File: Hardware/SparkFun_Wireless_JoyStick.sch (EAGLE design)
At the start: 76 parts, among them J7 CORTEX_DEBUGPTH, Q1 2.5A/30V, U1 JOYSTICKPTH, U2 JOYSTICKPTH, U3 74AHC1G125, U4 AP2112K-3.3V, U5 XBEE-2B3, U6 MAX1704X, U7 MCP73831, U8 ATSAMD21G-A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

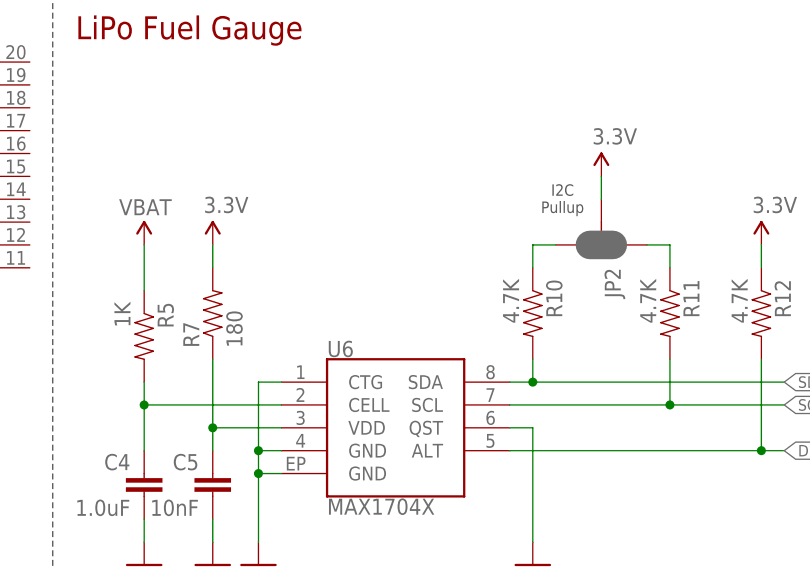
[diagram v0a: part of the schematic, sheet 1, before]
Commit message: Added fuel gauge i2c address
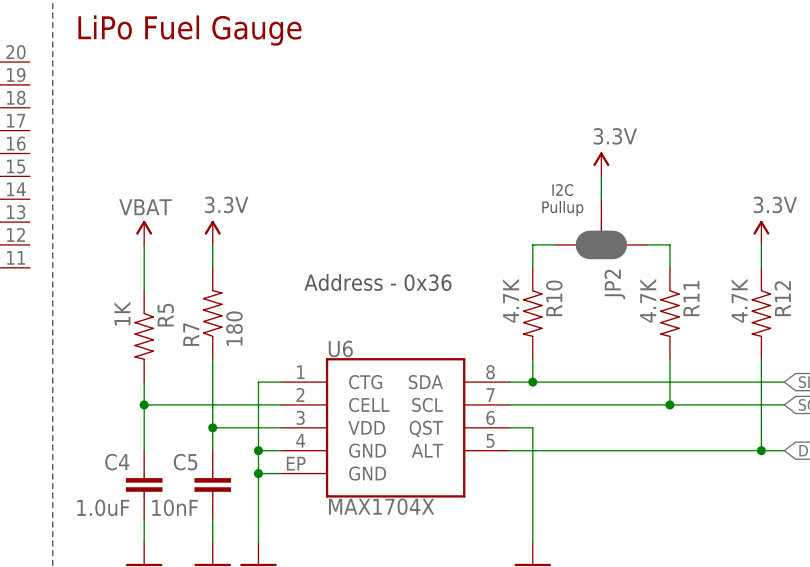
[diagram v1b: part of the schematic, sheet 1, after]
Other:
- note added: "Address - 0x36"
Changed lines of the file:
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@@
 <text x="193.04" y="137.16" size="1.27" layer="97" align="bottom-center">Charge Current
 Select</text>
+<text x="185.42" y="76.2" size="1.778" layer="97">Address - 0x36</text>
 </plain>
 <instances>

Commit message: Minor Changes
- added reset switch
- reversed power and ground on joysticks
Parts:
- added S8: MOMENTARY-SWITCH-SPST-SMD-4.6X2.8MM, SparkFun-Switches:MOMENTARY-SWITCH-SPST-SMD-4.6X2.8MM
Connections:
- net !RESET: now also S8.1
- net 3.3V: now also U1.H-, U1.V-, U2.H-, U2.V-; no longer U1.H+, U1.V+, U2.H+, U2.V+
- net GND: now also S8.2, U1.H+, U1.V+, U2.H+, U2.V+; no longer U1.H-, U1.V-, U2.H-, U2.V-
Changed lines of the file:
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@@
 <part name="SUPPLY23" library="SparkFun-Aesthetics" deviceset="VIN" device=""/>
 <part name="GND30" library="SparkFun-Aesthetics" deviceset="GND" device=""/>
+<part name="S8" library="SparkFun-Switches" deviceset="MOMENTARY-SWITCH-SPST" device="-SMD-4.6X2.8MM" value=""/>
+<part name="GND31" library="SparkFun-Aesthetics" deviceset="GND" device=""/>
 </parts>
 <sheets>
@@
 </segment>
 <segment>
-<pinref part="U2" gate="G$1" pin="V-"/>
-<wire x1="50.8" y1="106.68" x2="53.34" y2="106.68" width="0.1524" layer="91"/>
-<wire x1="53.34" y1="106.68" x2="53.34" y2="96.52" width="0.1524" layer="91"/>
-<pinref part="U2" gate="G$1" pin="H-"/>
-<wire x1="53.34" y1="96.52" x2="50.8" y2="96.52" width="0.1524" layer="91"/>
 <pinref part="U2" gate="G$1" pin="SEL-"/>
 <wire x1="50.8" y1="88.9" x2="53.34" y2="88.9" width="0.1524" layer="91"/>
-<wire x1="53.34" y1="88.9" x2="53.34" y2="96.52" width="0.1524" layer="91"/>
-<junction x="53.34" y="96.52"/>
 <wire x1="53.34" y1="88.9" x2="53.34" y2="81.28" width="0.1524" layer="91"/>
+<pinref part="GND5" gate="1" pin="GND"/>
+<pinref part="U2" gate="G$1" pin="V+"/>
+<wire x1="50.8" y1="111.76" x2="53.34" y2="111.76" width="0.1524" layer="91"/>
+<wire x1="53.34" y1="111.76" x2="53.34" y2="101.6" width="0.1524" layer="91"/>
+<pinref part="U2" gate="G$1" pin="H+"/>
+<wire x1="53.34" y1="101.6" x2="50.8" y2="101.6" width="0.1524" layer="91"/>
+<wire x1="53.34" y1="101.6" x2="53.34" y2="88.9" width="0.1524" layer="91"/>
+<junction x="53.34" y="101.6"/>
 <junction x="53.34" y="88.9"/>
-<pinref part="GND5" gate="1" pin="GND"/>
-</segment>
-<segment>
-<pinref part="U1" gate="G$1" pin="V-"/>
-<wire x1="20.32" y1="106.68" x2="22.86" y2="106.68" width="0.1524" layer="91"/>
-<wire x1="22.86" y1="106.68" x2="22.86" y2="96.52" width="0.1524" layer="91"/>
+</segment>
+<segment>
 <pinref part="U1" gate="G$1" pin="SEL-"/>
-<wire x1="22.86" y1="96.52" x2="22.86" y2="88.9" width="0.1524" layer="91"/>
 <wire x1="22.86" y1="88.9" x2="22.86" y2="81.28" width="0.1524" layer="91"/>
 <wire x1="20.32" y1="88.9" x2="22.86" y2="88.9" width="0.1524" layer="91"/>
+<pinref part="GND2" gate="1" pin="GND"/>
+<pinref part="U1" gate="G$1" pin="H+"/>
+<wire x1="20.32" y1="101.6" x2="22.86" y2="101.6" width="0.1524" layer="91"/>
+<wire x1="22.86" y1="101.6" x2="22.86" y2="111.76" width="0.1524" layer="91"/>
+<pinref part="U1" gate="G$1" pin="V+"/>
+<wire x1="22.86" y1="111.76" x2="20.32" y2="111.76" width="0.1524" layer="91"/>
+<wire x1="22.86" y1="101.6" x2="22.86" y2="88.9" width="0.1524" layer="91"/>
+<junction x="22.86" y="101.6"/>
 <junction x="22.86" y="88.9"/>
-<pinref part="U1" gate="G$1" pin="H-"/>
-<wire x1="20.32" y1="96.52" x2="22.86" y2="96.52" width="0.1524" layer="91"/>
-<junction x="22.86" y="96.52"/>
-<pinref part="GND2" gate="1" pin="GND"/>
 </segment>
 <segment>
@@
 <net name="3.3V" class="0">
 <segment>
-<pinref part="U2" gate="G$1" pin="H+"/>
-<wire x1="50.8" y1="101.6" x2="55.88" y2="101.6" width="0.1524" layer="91"/>
-<wire x1="55.88" y1="101.6" x2="55.88" y2="111.76" width="0.1524" layer="91"/>
-<pinref part="U2" gate="G$1" pin="V+"/>
-<wire x1="55.88" y1="111.76" x2="55.88" y2="114.3" width="0.1524" layer="91"/>
-<wire x1="50.8" y1="111.76" x2="55.88" y2="111.76" width="0.1524" layer="91"/>
-<junction x="55.88" y="111.76"/>
-<pinref part="SUPPLY3" gate="G$1" pin="3.3V"/>
-</segment>
-<segment>
-<pinref part="U1" gate="G$1" pin="H+"/>
-<wire x1="20.32" y1="101.6" x2="25.4" y2="101.6" width="0.1524" layer="91"/>
-<wire x1="25.4" y1="101.6" x2="25.4" y2="111.76" width="0.1524" layer="91"/>
-<pinref part="U1" gate="G$1" pin="V+"/>
-<wire x1="25.4" y1="111.76" x2="25.4" y2="114.3" width="0.1524" layer="91"/>
-<wire x1="20.32" y1="111.76" x2="25.4" y2="111.76" width="0.1524" layer="91"/>
-<junction x="25.4" y="111.76"/>
-<pinref part="SUPPLY2" gate="G$1" pin="3.3V"/>
-</segment>
-<segment>
 <pinref part="J4" gate="G$1" pin="2"/>
 <wire x1="83.82" y1="55.88" x2="78.74" y2="55.88" width="0.1524" layer="91"/>
@@
 <wire x1="106.68" y1="101.6" x2="106.68" y2="109.22" width="0.1524" layer="91"/>
 <pinref part="SUPPLY8" gate="G$1" pin="3.3V"/>
+</segment>
+<segment>
+<pinref part="U1" gate="G$1" pin="V-"/>
+<pinref part="SUPPLY2" gate="G$1" pin="3.3V"/>
+<wire x1="20.32" y1="106.68" x2="25.4" y2="106.68" width="0.1524" layer="91"/>
+<wire x1="25.4" y1="106.68" x2="25.4" y2="114.3" width="0.1524" layer="91"/>
+<pinref part="U1" gate="G$1" pin="H-"/>
+<wire x1="20.32" y1="96.52" x2="25.4" y2="96.52" width="0.1524" layer="91"/>
+<wire x1="25.4" y1="96.52" x2="25.4" y2="106.68" width="0.1524" layer="91"/>
+<junction x="25.4" y="106.68"/>
+</segment>
+<segment>
+<pinref part="U2" gate="G$1" pin="V-"/>
+<pinref part="SUPPLY3" gate="G$1" pin="3.3V"/>
+<wire x1="50.8" y1="106.68" x2="55.88" y2="106.68" width="0.1524" layer="91"/>
+<wire x1="55.88" y1="106.68" x2="55.88" y2="114.3" width="0.1524" layer="91"/>
+<pinref part="U2" gate="G$1" pin="H-"/>
+<wire x1="50.8" y1="96.52" x2="55.88" y2="96.52" width="0.1524" layer="91"/>
+<wire x1="55.88" y1="96.52" x2="55.88" y2="106.68" width="0.1524" layer="91"/>
+<junction x="55.88" y="106.68"/>
 </segment>
 </net>
@@
 <instance part="R16" gate="G$1" x="218.44" y="68.58" rot="R90"/>
 <instance part="GND28" gate="1" x="218.44" y="48.26"/>
+<instance part="S8" gate="G$1" x="30.48" y="25.4"/>
+<instance part="GND31" gate="1" x="38.1" y="20.32"/>
 </instances>
 <busses>
@@
 <wire x1="218.44" y1="53.34" x2="218.44" y2="50.8" width="0.1524" layer="91"/>
 </segment>
+<segment>
+<pinref part="S8" gate="G$1" pin="2"/>
+<wire x1="35.56" y1="25.4" x2="38.1" y2="25.4" width="0.1524" layer="91"/>
+<wire x1="38.1" y1="25.4" x2="38.1" y2="22.86" width="0.1524" layer="91"/>
+<pinref part="GND31" gate="1" pin="GND"/>
+</segment>
 </net>
 <net name="3.3V" class="0">
@@
 <label x="198.12" y="106.68" size="1.27" layer="95" rot="R180" xref="yes"/>
 </segment>
-</net>
+<segment>
+<pinref part="S8" gate="G$1" pin="1"/>
+<wire x1="25.4" y1="25.4" x2="22.86" y2="25.4" width="0.1524" layer="91"/>
+<label x="22.86" y="25.4" size="1.27" layer="95" rot="R180" xref="yes"/>
+</segment>
+</net>
